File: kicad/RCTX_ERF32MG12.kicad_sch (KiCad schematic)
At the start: 95 parts, among them J20 USB_OTG, J21 USB, J22 USB, P10 LEDs, P6 SD Card, P9 BUZZ, SW1 SW_Push-switches, U1 MAX2650, U10 ATSAMD11D14A-M, U11 USB6B1, U12 MAX2650

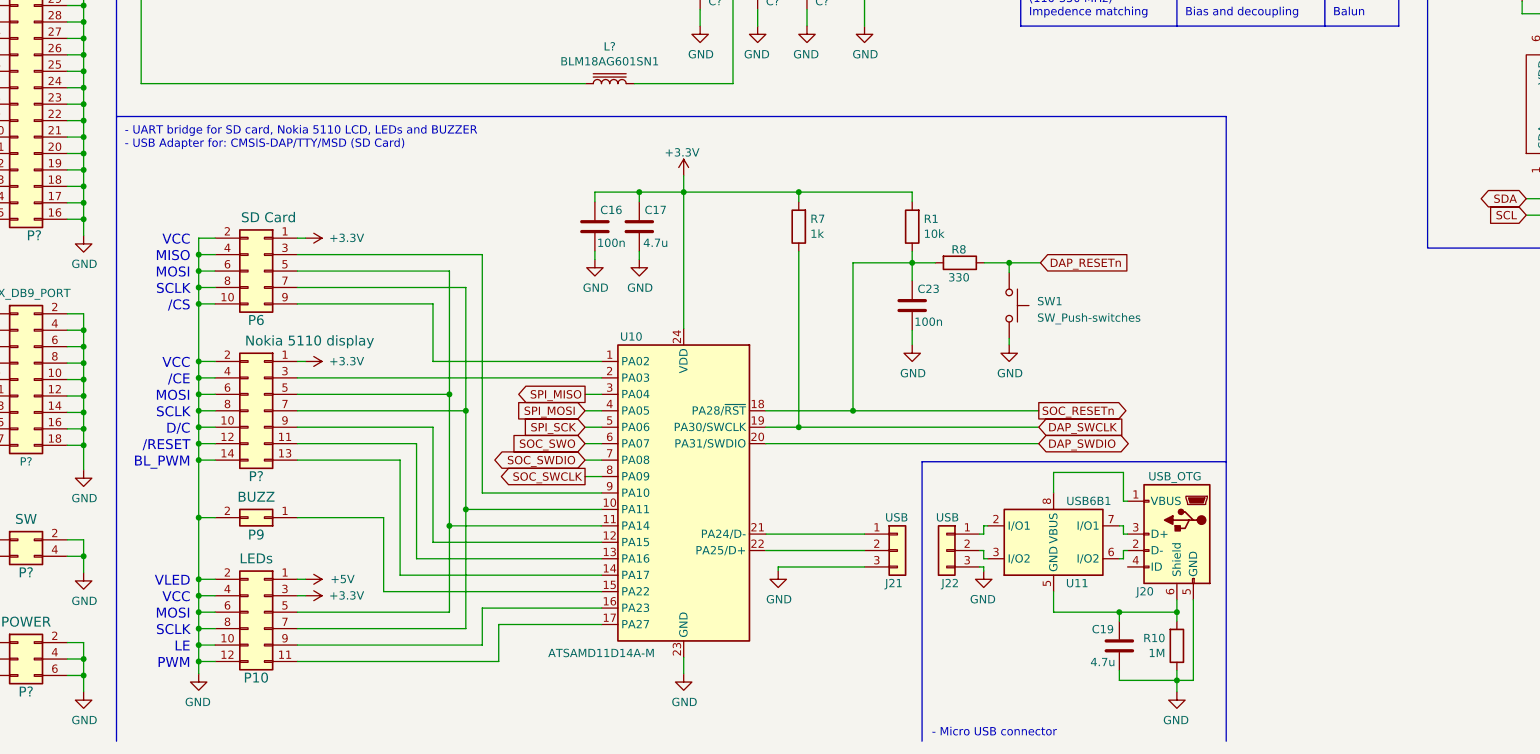
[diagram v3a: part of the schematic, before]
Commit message: Using EFM32HG310-QFN32 instead of SAMD11D14M for USB bridge - updating schematics
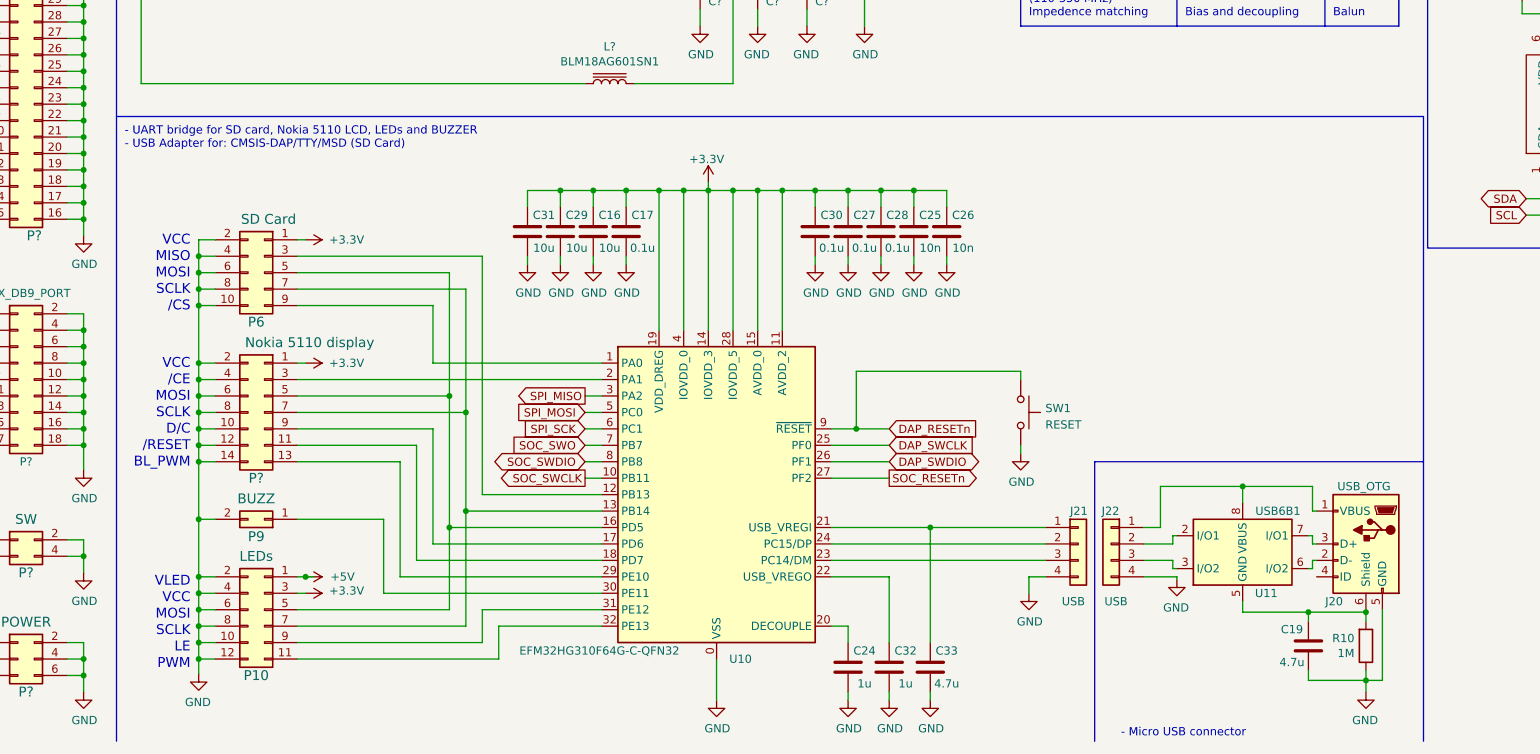
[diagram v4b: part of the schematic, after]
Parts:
- removed C23: 100n, symbol device:C
- removed J21, J22: USB, symbol Connector_Generic:Conn_01x03
- removed R1: 10k, symbol device:R
- removed R7: 1k, symbol device:R
- removed R8: 330, symbol device:R
- removed U10: ATSAMD11D14A-M, Package_DFN_QFN:QFN-24-1EP_4x4mm_P0.5mm_EP2.6x2.6mm, symbol MCU_Microchip_SAMD:ATSAMD11D14A-M
- added C24, C32: 1u, symbol device:C
- added C25, C26: 10n, symbol device:C
- added C27, C28, C30: 0.1u, symbol device:C
- added C29, C31: 10u, symbol device:C
- added C33: 4.7u, symbol device:C
- added J21, J22: USB, symbol Connector_Generic:Conn_01x04
- added U10: EFM32HG310F64G-C-QFN32, Package_DFN_QFN:QFN-32-1EP_6x6mm_P0.65mm_EP4.4x4.4mm, symbol EFM32HG310-QFN32:EFM32HG310F64G-C-QFN32
- C16: value 100n -> 10u
- C17: value 4.7u -> 0.1u
- SW1: value SW_Push-switches -> RESET
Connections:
- net +3V3: now also C25.2, C26.2, C27.2, C28.2, C29.2, C30.2, C31.2, U10.11 (AVDD_2), U10.14 (IOVDD_3), U10.15 (AVDD_0), U10.19 (VDD_DREG), U10.28 (IOVDD_5), U10.4 (IOVDD_0)
- net DAP_RESETn: now also U10.9 (~{RESET})
- net DAP_SWCLK: now also U10.25 (PF0)
- net DAP_SWDIO: now also U10.26 (PF1)
- net GND: now also C24.1, C25.1, C26.1, C27.1, C28.1, C29.1, C30.1, C31.1, C32.1, C33.1, J21.4 (Pin_4), J22.4 (Pin_4), U10.0 (VSS)
- net SOC_RESETn: now also U10.27 (PF2)
- net SOC_SWCLK: now also U10.10 (PB11)
- net SOC_SWDIO: now also U10.8 (PB8)
- net SOC_SWO: now also U10.7 (PB7)
- net SPI_MISO: now also U10.3 (PA2)
- net SPI_MOSI: now also U10.5 (PC0)
- net SPI_SCK: now also U10.6 (PC1)
- net at J20.1 (VBUS), U11.1 (VBUS), U11.8 (VBUS): now also J22.1 (Pin_1)
- net at U11.2 (I/O1): now also J22.2 (Pin_2)
- net at U11.3 (I/O2): now also J22.3 (Pin_3)
- net at P10.11 (Pin_11): now also U10.32 (PE13)
- net at P10.5 (Pin_5), P6.5 (Pin_5), P?.5 (Pin_5): now also U10.16 (PD5)
- net at P10.7 (Pin_7), P6.7 (Pin_7), P?.7 (Pin_7): now also U10.13 (PB14)
- net at P10.9 (Pin_9): now also U10.31 (PE12)
- net at P6.9 (Pin_9): now also U10.1 (PA0)
- net at P?.9 (Pin_9): now also U10.17 (PD6)
- net at P?.11 (Pin_11): now also U10.18 (PD7)
- net at P?.13 (Pin_13): now also U10.29 (PE10)
- net at P9.1 (Pin_1): now also U10.30 (PE11)
- net at P?.3 (Pin_3): now also U10.2 (PA1)
- net at P6.3 (Pin_3): now also U10.12 (PB13)
- new net: C24.2, U10.20 (DECOUPLE)
- new net: C33.2, J21.1 (Pin_1), U10.21 (USB_VREGI)
- new net: C32.2, U10.22 (USB_VREGO)
- new net: J21.3 (Pin_3), U10.23 (PC14/DM)
- new net: J21.2 (Pin_2), U10.24 (PC15/DP)
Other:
- moved on the sheet: C16, C17, C19, J20, R10, SW1, U11

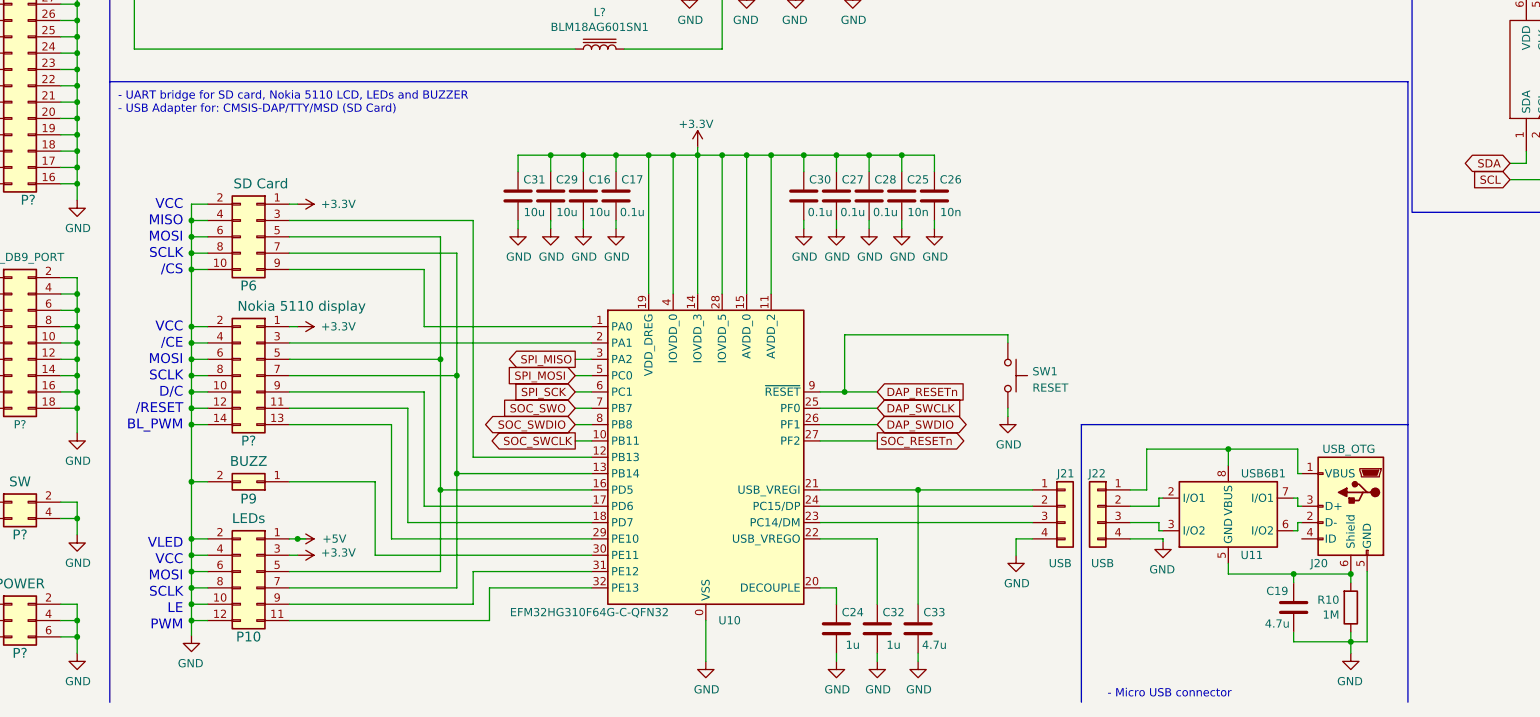
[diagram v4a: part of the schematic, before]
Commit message: Using 8x4 sqaure symbol for EFM32HG310-QFN32
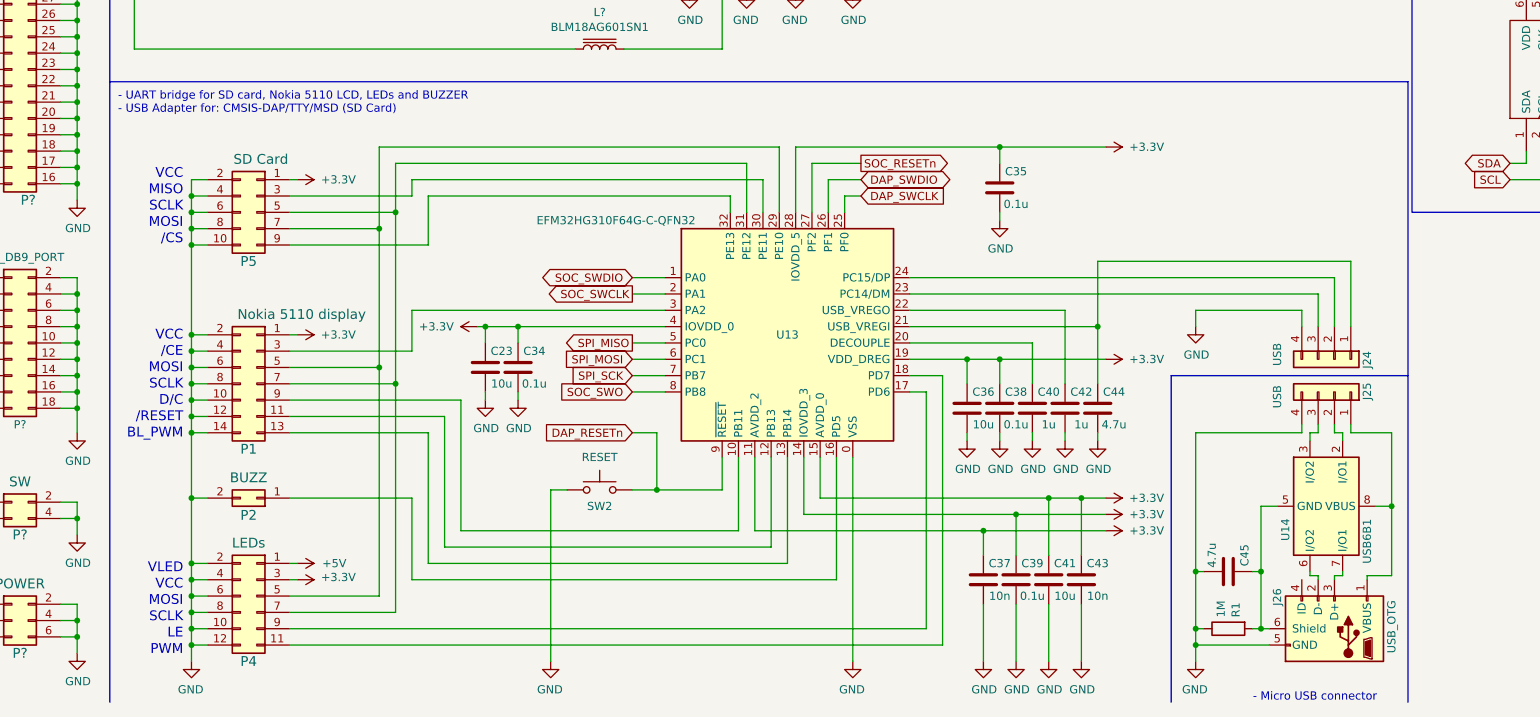
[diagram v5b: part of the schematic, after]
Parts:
- removed C16, C29, C31: 10u, symbol device:C
- removed C17, C27, C28, C30: 0.1u, symbol device:C
- removed C19, C33: 4.7u, symbol device:C
- removed C24, C32: 1u, symbol device:C
- removed C25, C26: 10n, symbol device:C
- removed J20: USB_OTG, symbol conn:USB_OTG
- removed J21, J22: USB, symbol Connector_Generic:Conn_01x04
- removed P10: LEDs, symbol conn:Conn_02x06_Odd_Even
- removed P6: SD Card, symbol conn:Conn_02x05_Odd_Even
- removed P9: BUZZ, symbol conn:Conn_02x01
- removed P?: Nokia 5110 display, symbol Connector_Generic:Conn_02x07_Odd_Even
- removed R10: 1M, symbol device:R
- removed SW1: RESET, symbol RCTX-rescue:SW_Push-switches
- removed U10: EFM32HG310F64G-C-QFN32, Package_DFN_QFN:QFN-32-1EP_6x6mm_P0.65mm_EP4.4x4.4mm, symbol EFM32HG310-QFN32:EFM32HG310F64G-C-QFN32
- removed U11: USB6B1, Package_SO:SOIC-8_3.9x4.9mm_P1.27mm, symbol Power_Protection:USB6B1
- added C23, C36, C41: 10u, symbol device:C
- added C34, C35, C38, C39: 0.1u, symbol device:C
- added C37, C43: 10n, symbol device:C
- added C40, C42: 1u, symbol device:C
- added C44, C45: 4.7u, symbol device:C
- added J24, J25: USB, symbol Connector_Generic:Conn_01x04
- added J26: USB_OTG, symbol conn:USB_OTG
- added P1: Nokia 5110 display, symbol Connector_Generic:Conn_02x07_Odd_Even
- added P2: BUZZ, symbol conn:Conn_02x01
- added P4: LEDs, symbol conn:Conn_02x06_Odd_Even
- added P5: SD Card, symbol conn:Conn_02x05_Odd_Even
- added R1: 1M, symbol device:R
- added SW2: RESET, symbol RCTX-rescue:SW_Push-switches
- added U13: EFM32HG310F64G-C-QFN32, Package_DFN_QFN:QFN-32-1EP_6x6mm_P0.65mm_EP4.4x4.4mm, symbol EFM32HG310-QFN32:EFM32HG310F64G-C-QFN32_1
- added U14: USB6B1, Package_SO:SOIC-8_3.9x4.9mm_P1.27mm, symbol Power_Protection:USB6B1
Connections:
- net +3V3: now also C23.2, C34.2, C35.2, C36.2, C37.2, C38.2, C39.2, C41.2, C43.2, P1.1 (Pin_1), P4.3 (Pin_3), P5.1 (Pin_1), U13.11 (AVDD_2), U13.14 (IOVDD_3), U13.15 (AVDD_0), U13.19 (VDD_DREG), U13.28 (IOVDD_5), U13.4 (IOVDD_0)
- net +5V: now also P4.1 (Pin_1)
- net DAP_RESETn: now also SW2.2, U13.9 (~{RESET})
- net DAP_SWCLK: now also U13.25 (PF0)
- net DAP_SWDIO: now also U13.26 (PF1)
- net GND: now also C23.1, C34.1, C35.1, C36.1, C37.1, C38.1, C39.1, C40.1, C41.1, C42.1, C43.1, C44.1, C45.1, J24.4 (Pin_4), J25.4 (Pin_4), J26.5 (GND), P1.10 (Pin_10), P1.12 (Pin_12), P1.14 (Pin_14), P1.2 (Pin_2), P1.4 (Pin_4), P1.6 (Pin_6), P1.8 (Pin_8), P2.2 (Pin_2), P4.10 (Pin_10), P4.12 (Pin_12), P4.2 (Pin_2), P4.4 (Pin_4), P4.6 (Pin_6), P4.8 (Pin_8), P5.10 (Pin_10), P5.2 (Pin_2), P5.4 (Pin_4), P5.6 (Pin_6), P5.8 (Pin_8), R1.1, SW2.1, U13.0 (VSS)
- net SOC_RESETn: now also U13.27 (PF2)
- net SOC_SWCLK: now also U13.2 (PA1)
- net SOC_SWDIO: now also U13.1 (PA0)
- net SOC_SWO: now also U13.8 (PB8)
- net SPI_MISO: now also U13.5 (PC0)
- net SPI_MOSI: now also U13.6 (PC1)
- net SPI_SCK: now also U13.7 (PB7)
- new net: C45.2, J26.6 (Shield), R1.2, U14.4 (GND), U14.5 (GND)
- new net: C44.2, J24.1 (Pin_1), U13.21 (USB_VREGI)
- new net: J24.2 (Pin_2), U13.24 (PC15/DP)
- new net: J24.3 (Pin_3), U13.23 (PC14/DM)
- new net: C40.2, U13.20 (DECOUPLE)
- new net: P4.11 (Pin_11), U13.18 (PD7)
- new net: P1.5 (Pin_5), P4.5 (Pin_5), P5.7 (Pin_7), U13.29 (PE10)
- new net: P1.7 (Pin_7), P4.7 (Pin_7), P5.5 (Pin_5), U13.31 (PE12)
- new net: P4.9 (Pin_9), U13.17 (PD6)
- new net: P1.11 (Pin_11), U13.12 (PB13)
- new net: P1.13 (Pin_13), U13.13 (PB14)
- new net: P1.3 (Pin_3), U13.3 (PA2)
- new net: P1.9 (Pin_9), U13.10 (PB11)
- new net: P2.1 (Pin_1), U13.16 (PD5)
- new net: C42.2, U13.22 (USB_VREGO)
- new net: P5.3 (Pin_3), U13.30 (PE11)
- new net: P5.9 (Pin_9), U13.32 (PE13)
- new net: J25.1 (Pin_1), J26.1 (VBUS), U14.1 (VBUS), U14.8 (VBUS)
- new net: J26.2 (D-), U14.6 (I/O2)
- new net: J26.3 (D+), U14.7 (I/O1)
- new net: J25.2 (Pin_2), U14.2 (I/O1)
- new net: J25.3 (Pin_3), U14.3 (I/O2)
